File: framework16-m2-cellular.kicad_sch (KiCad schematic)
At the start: 88 parts, among them J1 M.2 Socket B-Key (2199230-3), J10 MHF4L (20579-001E), J11 SIM Card, J12 Fan 1, J13 Fan 2, J2 u.FL, J3 MHF4L (20579-001E), J5 u.FL, J6 MHF4L (20579-001E), J7 u.FL, J8 MHF4L (20579-001E), J9 u.FL, Q1 NPN, U1 BR24G32FVT-3, U2 TCA9534, U3 74LVC1G11, U4 LTC6994xS6-1, U5 TPS628304ARZER

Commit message: Version v1.1
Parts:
- added R9: 1K, Resistor_SMD:R_0603_1608Metric, symbol Device:R
- added TP11, TP12, TP15: TestPoint, TestPoint:TestPoint_Pad_D1.0mm, symbol Connector:TestPoint
- renumbered R7 to R1, R9 to R10, R10 to R11, R11 to R12, R12 to R13, R13 to R14, R14 to R15, R15 to R16, R16 to R17, R17 to R18, R18 to R19, R19 to R20, R20 to R21, R21 to R22, R22 to R23, R23 to R24, R1 to R7, TP11 to TP13, TP12 to TP14
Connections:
- net +3.3V: now also TP12.1
- net GND: now also TP15.1
- net POWER_ON: now also TP11.1
- net RESET: now also R9.1; no longer Q1.1 (B), R10.1
- new net: Q1.1 (B), R10.1, R9.2
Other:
- moved on the sheet: C15, C16, R14, R16, R17, R8, U3, U4

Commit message: Bunch of improvements for v1.1
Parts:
- added HS1: M.2 Thermal Pads, FW16Cellular:Thermal Pad, symbol Mechanical:Heatsink_Pad
- J2, J5, J7, J9: value u.FL -> MHF4L (20579-001E); footprint FW16Cellular:CONN_U.FL-R-SMT10_HIR -> FW16Cellular:CONN_20579-001E_IPX
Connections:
- net GND: now also HS1.1
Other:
- moved on the sheet: C1, C10, C11, C12, C13, C2, C3, C4, C5, C7, C8, C9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

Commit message: Fixes from v1.1
TODO: check the orientation of the fan headers
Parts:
- C13, C5: footprint Capacitor_SMD:CP_Elec_8x10 -> Capacitor_SMD:CP_Elec_6.3x5.4; LCSC C136294 -> C72494
- J12, J13: footprint FW16Cellular:A1001WR-S-04P -> FW16Cellular:AFC30-S04FCC-00; LCSC C371510 -> C395232
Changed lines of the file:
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@@
 			)
 		)
-		(property "Footprint" "FW16Cellular:A1001WR-S-04P"
+		(property "Footprint" "FW16Cellular:AFC30-S04FCC-00"
 			(at 34.29 222.25 0)
 			(effects
@@
 			)
 		)
-		(property "LCSC" "C371510"
+		(property "LCSC" "C395232"
 			(at 34.29 222.25 0)
 			(effects
@@
 			)
 		)
-		(property "Footprint" "FW16Cellular:A1001WR-S-04P"
+		(property "Footprint" "FW16Cellular:AFC30-S04FCC-00"
 			(at 34.29 246.38 0)
 			(effects
@@
 			)
 		)
-		(property "LCSC" "C371510"
+		(property "LCSC" "C395232"
 			(at 34.29 246.38 0)
 			(effects
@@
 			)
 		)
-		(property "Footprint" "Capacitor_SMD:CP_Elec_8x10"
+		(property "Footprint" "Capacitor_SMD:CP_Elec_6.3x5.4"
 			(at 358.14 36.83 0)
 			(effects
@@
 			)
 		)
-		(property "LCSC" "C136294"
+		(property "LCSC" "C72494"
 			(at 358.14 36.83 0)
 			(effects
@@
 			)
 		)
-		(property "Footprint" "Capacitor_SMD:CP_Elec_8x10"
+		(property "Footprint" "Capacitor_SMD:CP_Elec_6.3x5.4"
 			(at 378.46 55.88 0)
 			(effects
@@
 			)
 		)
-		(property "LCSC" "C136294"
+		(property "LCSC" "C72494"
 			(at 378.46 55.88 0)
 			(effects

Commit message: Remove EEPROM address jumper
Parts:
- removed JP1: SolderJumper_3_Bridged12, Jumper:SolderJumper-3_P1.3mm_Bridged12_RoundedPad1.0x1.5mm, symbol Jumper:SolderJumper_3_Bridged12
- renumbered JP2 to JP1
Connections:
- net GND: now also U1.1 (A0), U1.2 (A1), U1.3 (A2)
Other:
- moved on the sheet: C6, U1

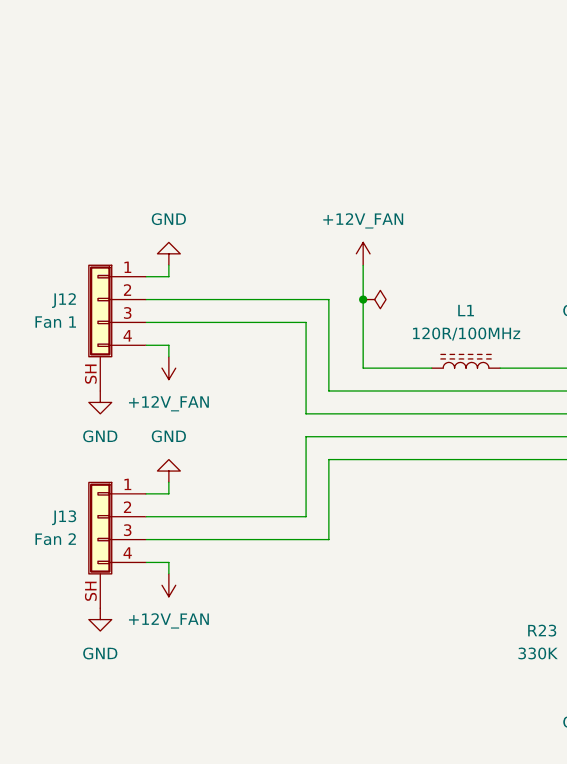
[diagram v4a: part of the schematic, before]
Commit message: Fix flipped fan connector
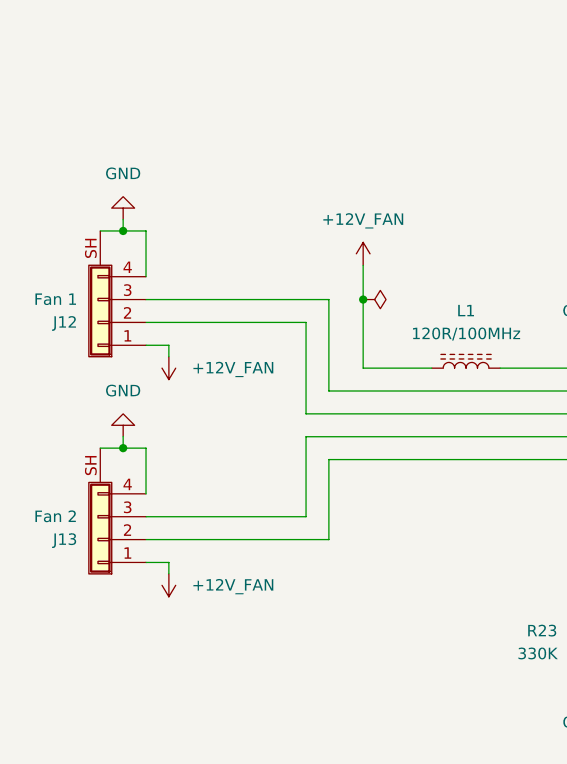
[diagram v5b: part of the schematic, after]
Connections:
- net +12V_FAN: now also J12.1 (Pin_1), J13.1 (Pin_1); no longer J12.4 (Pin_4), J13.4 (Pin_4)
- net GND: now also J12.4 (Pin_4), J13.4 (Pin_4); no longer J12.1 (Pin_1), J13.1 (Pin_1)
- net at J12.2 (Pin_2): now also J4.PH2 (Fan0_SPEED); no longer J4.PL5 (Fan0_PWM)
- net at J12.3 (Pin_3): now also J4.PL5 (Fan0_PWM); no longer J4.PH2 (Fan0_SPEED)
- net at J13.2 (Pin_2): now also J4.PJ2 (Fan1_SPEED); no longer J4.PK5 (Fan1_PWM)
- net at J13.3 (Pin_3): now also J4.PK5 (Fan1_PWM); no longer J4.PJ2 (Fan1_SPEED)
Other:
- moved on the sheet: J12, J13
